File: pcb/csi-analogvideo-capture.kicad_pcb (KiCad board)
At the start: 2 copper layers, 55 x 50 mm, 69 parts, among them CN1 rpi_camera_conn_top, J1 ANALOG_IN, U1 BD18KA5FP-E2, U2 ADV7280A-M, Y1 ABM8G-28.63636MHZ

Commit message: migrate to KiCAD 6.0, update schematic wip
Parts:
- TP1: value ~RESET -> ~{RESET}
- TP3: value ~INTRQ -> ~{INTRQ}
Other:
- net class Bold removed
- net class Default removed

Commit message: update schematicand pcb, DRC passed
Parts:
- removed CN1: rpi_camera_conn_top, Connector_FFC-FPC:TE_1-84953-5_1x15-1MP_P1.0mm_Horizontal
- removed D1: D, Diode_SMD:D_SOD-323_HandSoldering
- removed H1, H2, H3, H4: MountingHole, MountingHole:MountingHole_3.2mm_M3_ISO14580
- removed L1, L2, L3, L4, L5: FB, Inductor_SMD:L_0603_1608Metric_Pad1.05x0.95mm_HandSolder
- removed R22: 47Ω, Resistor_SMD:R_0603_1608Metric_Pad1.05x0.95mm_HandSolder
- added C30: 10nF, Capacitor_SMD:C_0402_1005Metric, B.Cu at (68.5, 59.0)
- added FB1: 600Ω, Inductor_SMD:L_0603_1608Metric, B.Cu at (57.9, 65.8)
- added FB2: 600Ω, Inductor_SMD:L_0603_1608Metric, B.Cu at (60.4, 65.0)
- added FB3: 600Ω, Inductor_SMD:L_0603_1608Metric, B.Cu at (70.8, 56.0)
- added FB4: 600Ω, Inductor_SMD:L_0603_1608Metric, B.Cu at (72.8, 61.1)
- added FB5: 600Ω, Inductor_SMD:L_0603_1608Metric, B.Cu at (72.8, 58.5)
- added J2: rpi_camera_conn_top, Connector_FFC-FPC:TE_1-84953-5_1x15-1MP_P1.0mm_Horizontal, F.Cu at (62.5, 73.0)
- added TP4: TestPoint, TestPoint:TestPoint_Pad_D1.0mm, F.Cu at (63.0, 64.0)
- added TP5: TestPoint, TestPoint:TestPoint_Pad_D1.0mm, F.Cu at (59.5, 68.3)
- added TP6: TestPoint, TestPoint:TestPoint_Pad_D1.0mm, F.Cu at (58.5, 67.3)
- C1, C16, C17, C18, C19, C2, C21, C22, C23, C24, C26, C27, C28, C29, C3, C4, C5, C6, C7, C8, C9: footprint Capacitor_SMD:C_0603_1608Metric_Pad1.05x0.95mm_HandSolder -> Capacitor_SMD:C_0402_1005Metric
- C10: value 20pF -> 4.7μF; footprint Capacitor_SMD:C_0603_1608Metric_Pad1.05x0.95mm_HandSolder -> Capacitor_SMD:C_0402_1005Metric
- C11: value 2.2μF -> 20pF; footprint Capacitor_SMD:C_0603_1608Metric_Pad1.05x0.95mm_HandSolder -> Capacitor_SMD:C_0402_1005Metric
- C12: value 47μF -> 0.1μF; footprint Capacitor_SMD:CP_Elec_5x5.3 -> Capacitor_SMD:C_0402_1005Metric
- C13: value 47μF -> 100μF; footprint Capacitor_SMD:CP_Elec_5x5.3 -> Capacitor_SMD:C_1206_3216Metric; moved to B.Cu
- C14: value 0.1μF -> 10nF; footprint Capacitor_SMD:C_0603_1608Metric_Pad1.05x0.95mm_HandSolder -> Capacitor_SMD:C_0402_1005Metric; moved to B.Cu
- C15: value 10μF -> 47μF; footprint Capacitor_SMD:C_0603_1608Metric_Pad1.05x0.95mm_HandSolder -> Capacitor_SMD:C_1206_3216Metric
- C20: value 0.1μF -> 10μF; footprint Capacitor_SMD:C_0603_1608Metric_Pad1.05x0.95mm_HandSolder -> Capacitor_SMD:C_0402_1005Metric
- C25: value 10nF -> 0.1μF; footprint Capacitor_SMD:C_0603_1608Metric_Pad1.05x0.95mm_HandSolder -> Capacitor_SMD:C_0402_1005Metric
- J1: value ANALOG_IN -> VIDEO_IN; footprint Connector_PinHeader_2.54mm:PinHeader_1x16_P2.54mm_Vertical -> Connector_PinHeader_2.54mm:PinHeader_2x08_P2.54mm_Vertical
- R1, R10, R11, R12, R13, R14, R15, R16, R17, R2, R20, R3, R4, R5, R6, R7, R8, R9: footprint Resistor_SMD:R_0603_1608Metric_Pad1.05x0.95mm_HandSolder -> Resistor_SMD:R_0402_1005Metric
- R18: value NI -> 560Ω; footprint Resistor_SMD:R_0603_1608Metric_Pad1.05x0.95mm_HandSolder -> Resistor_SMD:R_0402_1005Metric
- R19: footprint Resistor_SMD:R_0603_1608Metric_Pad1.05x0.95mm_HandSolder -> Resistor_SMD:R_0402_1005Metric; moved to F.Cu
- R21: value 560Ω -> DNP; footprint Resistor_SMD:R_0603_1608Metric_Pad1.05x0.95mm_HandSolder -> Resistor_SMD:R_0402_1005Metric
- TP1: value ~{RESET} -> TestPoint; footprint TestPoint:TestPoint_Pad_D1.5mm -> TestPoint:TestPoint_Pad_D1.0mm
- TP2: value GND -> TestPoint; footprint TestPoint:TestPoint_Pad_D1.5mm -> TestPoint:TestPoint_Pad_D1.0mm
- TP3: value ~{INTRQ} -> TestPoint; footprint TestPoint:TestPoint_Pad_D1.5mm -> TestPoint:TestPoint_Pad_D1.0mm
- U1: value BD18KA5FP-E2 -> ADV7280A-M; footprint Package_TO_SOT_SMD:TO-252-2 -> Package_CSP:LFCSP-32-1EP_5x5mm_P0.5mm_EP3.25x3.25mm
- U2: value ADV7280A-M -> NJM12888F18; footprint Package_CSP:LFCSP-32-1EP_5x5mm_P0.5mm_EP3.25x3.25mm -> Package_TO_SOT_SMD:SOT-23-5; moved to B.Cu
- Y1: footprint Crystal:Crystal_SMD_3225-4Pin_3.2x2.5mm_HandSoldering -> Crystal:Crystal_SMD_3225-4Pin_3.2x2.5mm
- moved C10 92.1 mm to (56.9, 54.1), turned to 180 degrees
- moved R21 84.3 mm to (56.9, 57.1), turned to 0 degrees
- moved C18 77.6 mm to (69.3, 55.7)
- moved C23 77.1 mm to (68.3, 55.7)
- moved C28 76.6 mm to (67.3, 55.7)
- moved C17 75.2 mm to (61.7, 63.7), turned to 0 degrees
- moved C9 74.4 mm to (70.6, 62.9)
- moved C22 74.1 mm to (61.7, 62.7), turned to 0 degrees
- moved Y1 73.4 mm to (71.2, 60.6)
- moved C27 73.1 mm to (61.7, 61.7), turned to 0 degrees
- moved C26 73.0 mm to (59.6, 61.0), turned to 180 degrees
- moved C1 72.3 mm to (70.0, 51.5), turned to 180 degrees
- moved R19 72.2 mm to (56.9, 55.1)
- moved C14 72.1 mm to (58.8, 73.0), turned to 0 degrees
- moved R1 72.0 mm to (69.5, 50.0)
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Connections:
- C10 pad 1: Net-(C10-Pad1) -> /~{RESET}
- C11 pad 1: Net-(C11-Pad1) -> /XTALN
- C12 pad 1: +3V3 -> Net-(C12-Pad1)
- C12 pad 2: GND -> Net-(C12-Pad2)
- C13 pad 1: +1V8 -> +3V3
- C14 pad 2: Net-(C14-Pad2) -> GND
- C15 pad 1: /DVDDIO_3V3 -> +1V8
- C16 pad 1: /DVDD_1V8 -> /DVDDIO_3V3
- C17 pad 1: /AVDD_1V8 -> /DVDD_1V8
- C18 pad 1: /MVDD_1V8 -> /AVDD_1V8
- C19 pad 1: /PVDD_1V8 -> /MVDD_1V8
- C20 pad 1: /DVDDIO_3V3 -> /PVDD_1V8
- C21 pad 1: /DVDD_1V8 -> /DVDDIO_3V3
- C22 pad 1: /AVDD_1V8 -> /DVDD_1V8
- C23 pad 1: /MVDD_1V8 -> /AVDD_1V8
- C24 pad 1: /PVDD_1V8 -> /MVDD_1V8
- C25 pad 1: /DVDDIO_3V3 -> /PVDD_1V8
- C26 pad 1: /DVDD_1V8 -> /DVDDIO_3V3
- C27 pad 1: /AVDD_1V8 -> /DVDD_1V8
- C28 pad 1: /MVDD_1V8 -> /AVDD_1V8
- C29 pad 1: /PVDD_1V8 -> /MVDD_1V8
- J1 pad 1: /P_AIN1 -> GND
- J1 pad 10: GND -> /VIN5
- J1 pad 11: /P_AIN6 -> GND
- J1 pad 12: GND -> /VIN6
- J1 pad 13: /P_AIN7 -> GND
- J1 pad 14: GND -> /VIN7
- J1 pad 15: /P_AIN8 -> GND
- J1 pad 16: GND -> /VIN8
- J1 pad 2: GND -> /VIN1
- J1 pad 3: /P_AIN2 -> GND
- J1 pad 4: GND -> /VIN2
- J1 pad 5: /P_AIN3 -> GND
- J1 pad 6: GND -> /VIN3
- J1 pad 7: /P_AIN4 -> GND
- J1 pad 8: GND -> /VIN4
- J1 pad 9: /P_AIN5 -> GND
- R1 pad 2: /P_AIN1 -> /VIN1
- R10 pad 1: Net-(C2-Pad2) -> GND
- R10 pad 2: GND -> Net-(C2-Pad2)
- R12 pad 1: Net-(C4-Pad2) -> GND
- R12 pad 2: GND -> Net-(C4-Pad2)
- R14 pad 1: Net-(C6-Pad2) -> GND
- R14 pad 2: GND -> Net-(C6-Pad2)
- R16 pad 1: Net-(C8-Pad2) -> GND
- R16 pad 2: GND -> Net-(C8-Pad2)
- R17 pad 1: Net-(R17-Pad1) -> /~{PWRDWN}
- R17 pad 2: +3V3 -> /DVDDIO_3V3
- R18 pad 1: GND -> Net-(C9-Pad1)
- R18 pad 2: Net-(R17-Pad1) -> /XTALP
- R19 pad 1: Net-(R19-Pad1) -> /~{RESET}
- R19 pad 2: +3V3 -> /DVDDIO_3V3
- R2 pad 2: /P_AIN2 -> /VIN2
- R20 pad 1: Net-(C11-Pad1) -> /ALSB
- R20 pad 2: +3V3 -> /DVDDIO_3V3
- R21 pad 1: Net-(R21-Pad1) -> GND
- R21 pad 2: Net-(C9-Pad1) -> /ALSB
- R3 pad 2: /P_AIN3 -> /VIN3
- R4 pad 2: /P_AIN4 -> /VIN4
- R5 pad 2: /P_AIN5 -> /VIN5
- R6 pad 2: /P_AIN6 -> /VIN6
- R7 pad 2: /P_AIN7 -> /VIN7
- R8 pad 2: /P_AIN8 -> /VIN8
- TP1 pad 1: Net-(R22-Pad2) -> /~{INTRQ}
- TP2 pad 1: GND -> /GPO2
- TP3 pad 1: Net-(TP3-Pad1) -> /GPO1
- U1 pad 1: +3V3 -> GND
- U1 pad 2: GND -> /DVDDIO_3V3
- U1 pad 3: +1V8 -> /DVDD_1V8
- U2 pad 1: GND -> +3V3
- U2 pad 2: /DVDDIO_3V3 -> GND
- U2 pad 3: /DVDD_1V8 -> +3V3
- U2 pad 4: GND -> Net-(C14-Pad1)
- U2 pad 5: Net-(TP3-Pad1) -> +1V8
- Y1 pad 3: Net-(C10-Pad1) -> /XTALN
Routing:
- net GND: track 45.3 -> 108.8 mm, vias 22 -> 24
- net +3V3: track 57.2 -> 18.6 mm
- net Net-(C11-Pad1): track 24.4 -> 0.00 mm
- net Net-(R17-Pad1): track 20.1 -> 0.00 mm
- net /AIN8: track 27.3 -> 8.65 mm
- net /AIN7: track 22.4 -> 6.97 mm
- net /AIN5: track 19.2 -> 5.25 mm
- net /DVDDIO_3V3: track 8.71 -> 22.1 mm, vias 1 -> 2
- net /AIN1: track 21.5 -> 8.18 mm
- net /AIN6: track 18.2 -> 5.37 mm
- net Net-(C10-Pad1): track 11.0 -> 0.00 mm
- net +1V8: track 53.4 -> 42.6 mm, vias 2 -> 0
- net Net-(R22-Pad2): track 10.6 -> 0.00 mm
- net /AIN4: track 15.1 -> 4.98 mm
- net /AIN2: track 17.3 -> 7.48 mm
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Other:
- board size 55 x 50 mm -> 25 x 40 mm
- rule pad_to_mask_clearance: 0.2 -> 0

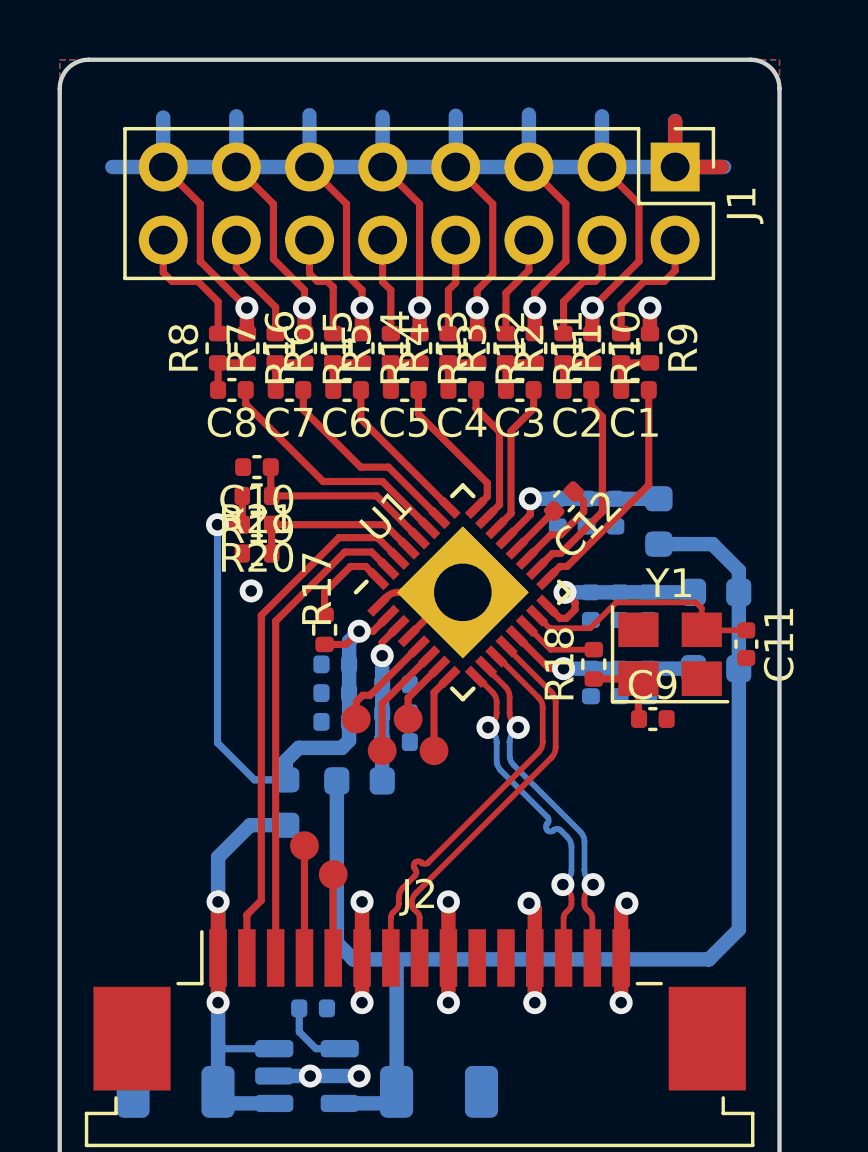
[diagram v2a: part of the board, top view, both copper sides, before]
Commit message: place silkscreen
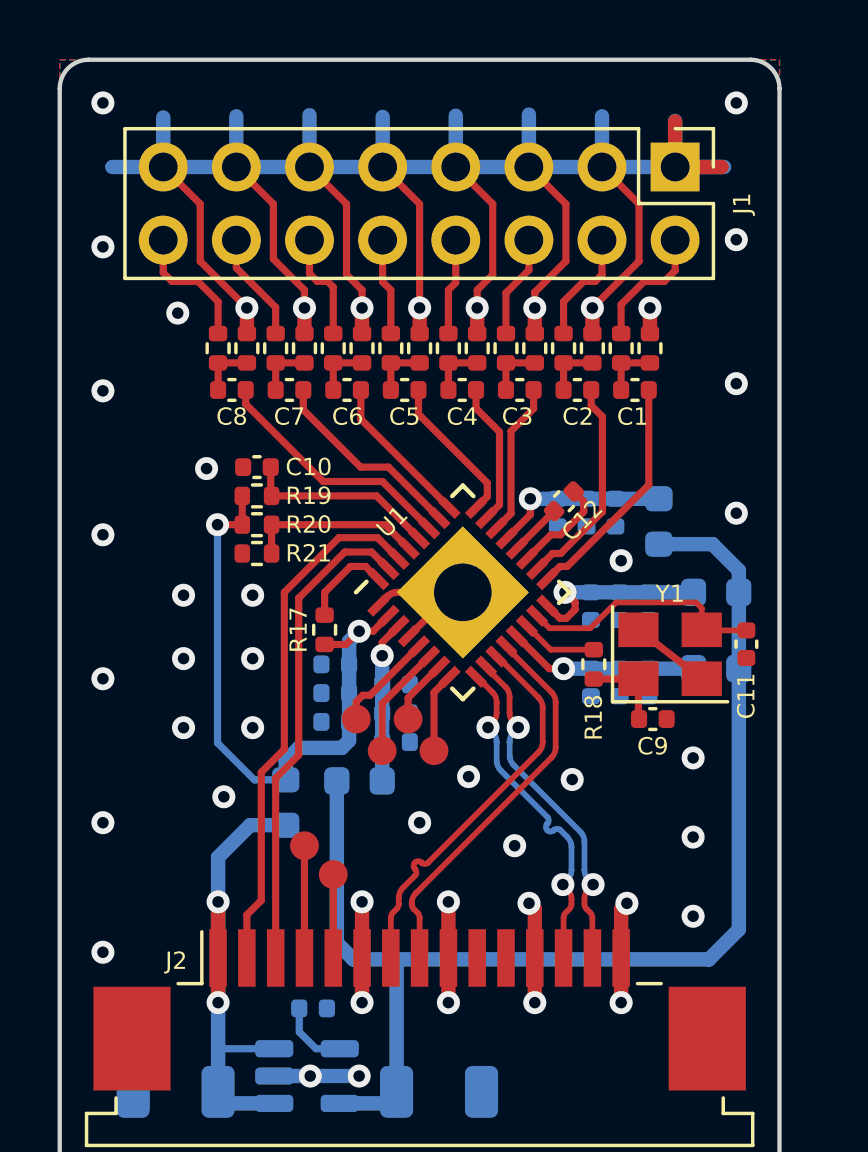
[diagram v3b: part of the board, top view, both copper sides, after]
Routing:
- net GND: track 108.8 -> 111.6 mm, vias 24 -> 51

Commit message: update pcb
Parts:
- moved C11 4.25 mm to (70.1, 58.3), turned to 0 degrees
- moved R18 3.05 mm to (70.2, 63.6), turned to 180 degrees
- moved C9 2.00 mm to (72.3, 61.9), turned to 90 degrees
- moved FB2 1.22 mm to (59.5, 65.8), turned to 90 degrees
- moved Y1 1.14 mm to (70.1, 61.0), turned to 90 degrees
- moved TP4 1.12 mm to (63.5, 63.0)
- moved FB3 1.10 mm to (71.6, 55.2), turned to 180 degrees
- moved TP2 1.04 mm to (60.9, 63.0)
- moved TP1 0.71 mm to (59.6, 63.0)
- moved TP3 0.14 mm to (62.2, 63.0)
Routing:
- net GND: track 111.6 -> 121.2 mm, vias 51 -> 52
- net /XTALN: track 8.66 -> 4.59 mm
- net /XTALP: track 2.66 -> 6.18 mm
- net +1V8: track 42.6 -> 40.5 mm
- net /DVDD_1V8: track 5.62 -> 6.89 mm
- net /GPO2: track 3.95 -> 3.07 mm
- net /GPO0: track 2.79 -> 1.96 mm
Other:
- board text added: "2022-07"
- board text added: "SDTV to CSI Video Decoder"

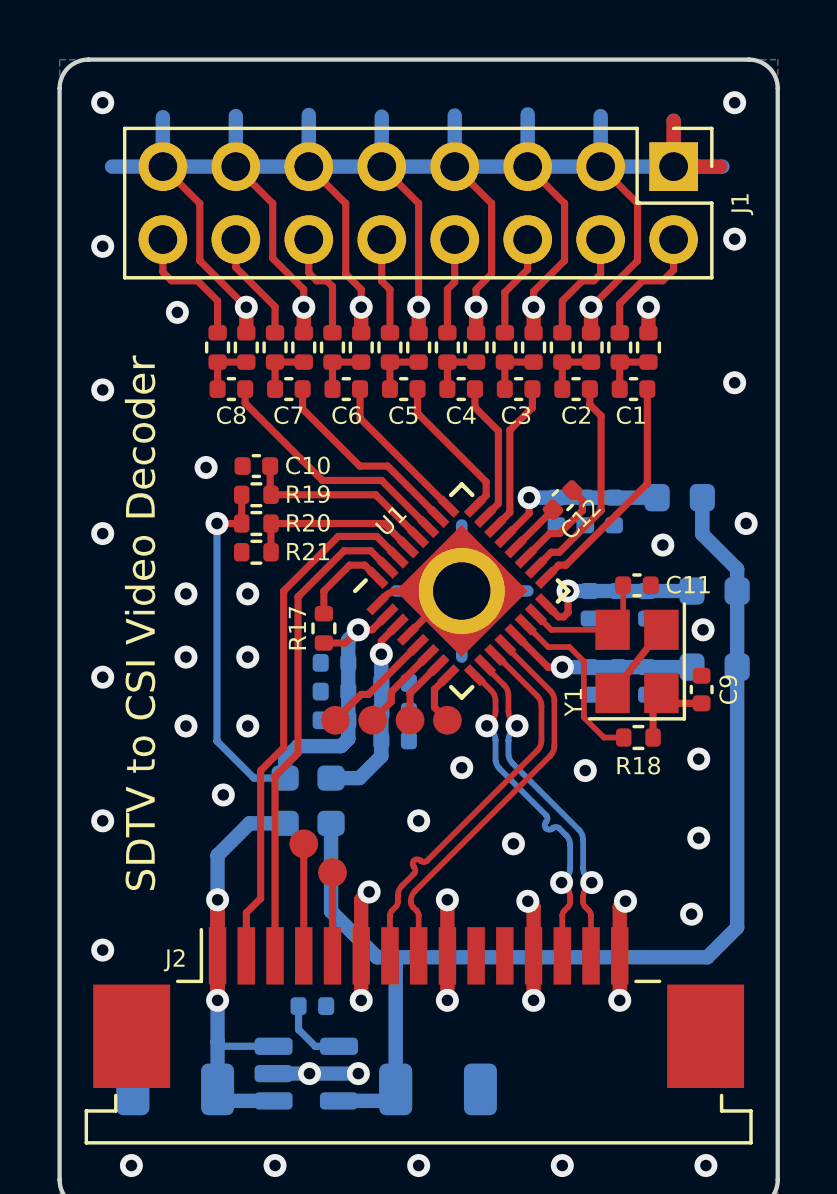
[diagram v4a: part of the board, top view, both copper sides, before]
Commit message: clean up project, update pcb
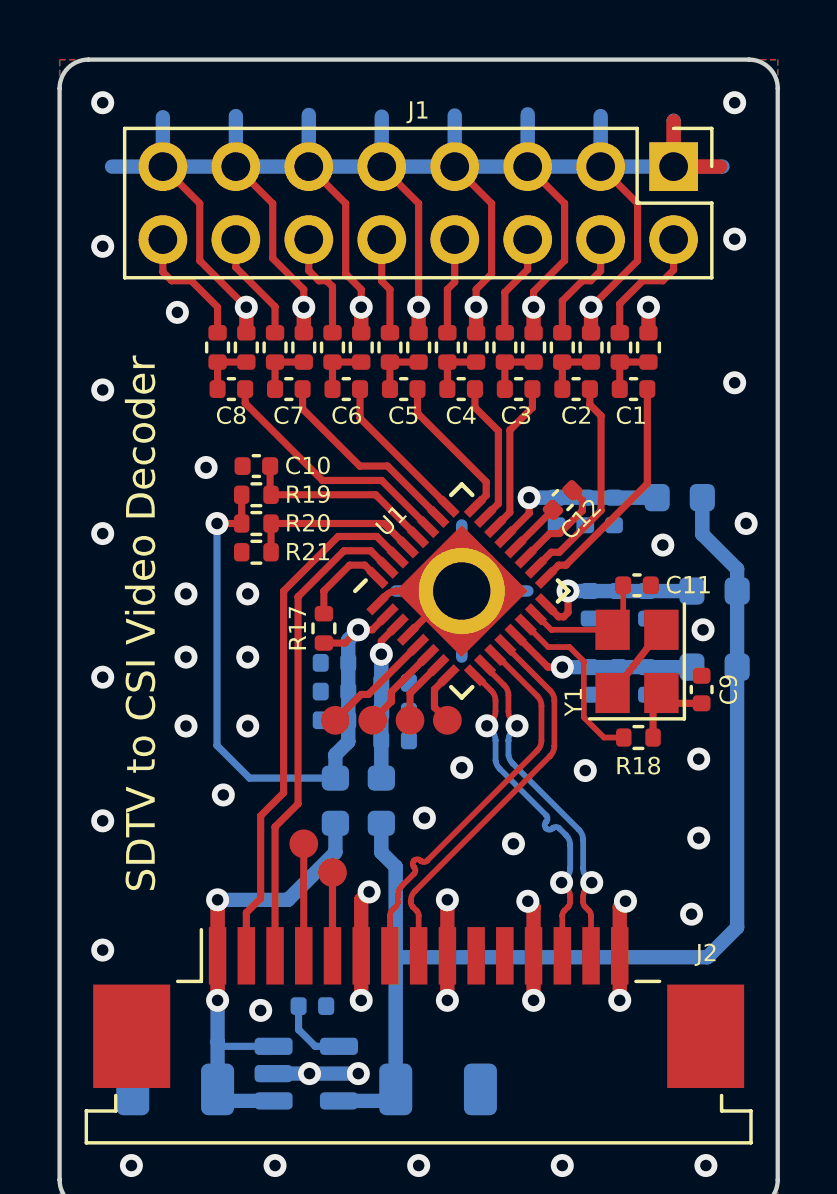
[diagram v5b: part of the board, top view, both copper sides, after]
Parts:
- J2: value rpi_camera_conn_top -> RPI_CSI_TOP
- moved FB1 1.75 mm to (59.6, 65.8)
- moved FB2 1.75 mm to (61.2, 65.8)
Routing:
- net +3V3: track 18.6 -> 20.0 mm
- net /DVDD_1V8: track 6.89 -> 5.58 mm
- net +1V8: track 40.5 -> 39.4 mm
- net GND: vias 52 -> 53
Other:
- board text added: "1"
- board text added: "2"
- board text added: "3"
- board text added: "4"
- board text added: "5"
- board text added: "6"
- board text added: "7"
- board text added: "8"
- board text added: "GND"
- board text added: "VIDEO IN"
